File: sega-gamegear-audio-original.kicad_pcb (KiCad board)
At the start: 2 copper layers, 57 x 31 mm, 22 parts, among them CN1 292161-6, CN2 CONN 2P, IC1 TDA2822D, J1 CONN MINI JACK

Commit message: update production files
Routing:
- net Net-(IC1-+I1): track 82.3 -> 81.7 mm
- net Net-(IC1-+I2): track 85.7 -> 85.2 mm
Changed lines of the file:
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@@
     (property "Sheetfile" "sega-gamegear-audio-original.kicad_sch")
     (property "Sheetname" "")
-    (attr through_hole exclude_from_pos_files)
+    (attr through_hole)
     (fp_text reference "CN1" (at -14 0.1) (layer "F.SilkS")
         (effects (font (size 1 1) (thickness 0.2) bold))
@@
     (property "Sheetfile" "sega-gamegear-audio-original.kicad_sch")
     (property "Sheetname" "")
-    (attr through_hole exclude_from_pos_files)
+    (attr through_hole)
     (fp_text reference "CN2" (at 0.9 2.9) (layer "F.SilkS")
         (effects (font (size 1 1) (thickness 0.2) bold))
@@
   (segment (start 70.264471 123.184471) (end 70.28 123.2) (width 0.25) (layer "F.Cu") (net 8))
   (segment (start 70.264471 121.6) (end 70.264471 123.184471) (width 0.57) (layer "F.Cu") (net 8))
-  (segment (start 99.07 118.581056) (end 99.069999 128.600945) (width 0.57) (layer "F.Cu") (net 9))
+  (segment (start 95.788944 115.3) (end 99.07 118.581056) (width 0.57) (layer "F.Cu") (net 9))
   (segment (start 86.50755 113.5695) (end 86.50755 114.70755) (width 0.57) (layer "F.Cu") (net 9))
   (segment (start 70.051056 127.44) (end 66.96211 127.439998) (width 0.57) (layer "F.Cu") (net 9))
+  (segment (start 58.622112 119.1) (end 51.1 119.1) (width 0.57) (layer "F.Cu") (net 9))
+  (segment (start 86.50755 114.70755) (end 87.1 115.3) (width 0.57) (layer "F.Cu") (net 9))
+  (segment (start 99.069999 127.618945) (end 96.848946 129.839998) (width 0.57) (layer "F.Cu") (net 9))
+  (segment (start 66.96211 127.439998) (end 58.622112 119.1) (width 0.57) (layer "F.Cu") (net 9))
+  (segment (start 99.07 118.581056) (end 99.069999 127.618945) (width 0.57) (layer "F.Cu") (net 9))
+  (segment (start 96.848946 129.839998) (end 72.451054 129.839998) (width 0.57) (layer "F.Cu") (net 9))
   (segment (start 72.451054 129.839998) (end 70.051056 127.44) (width 0.57) (layer "F.Cu") (net 9))
-  (segment (start 97.830946 129.839998) (end 72.451054 129.839998) (width 0.57) (layer "F.Cu") (net 9))
-  (segment (start 95.788944 115.3) (end 99.07 118.581056) (width 0.57) (layer "F.Cu") (net 9))
+  (segment (start 49 117) (end 49 112.5) (width 0.57) (layer "F.Cu") (net 9))
   (segment (start 87.1 115.3) (end 95.788944 115.3) (width 0.57) (layer "F.Cu") (net 9))
-  (segment (start 58.622112 119.1) (end 51.1 119.1) (width 0.57) (layer "F.Cu") (net 9))
-  (segment (start 49 117) (end 49 112.5) (width 0.57) (layer "F.Cu") (net 9))
-  (segment (start 86.50755 114.70755) (end 87.1 115.3) (width 0.57) (layer "F.Cu") (net 9))
-  (segment (start 66.96211 127.439998) (end 58.622112 119.1) (width 0.57) (layer "F.Cu") (net 9))
   (segment (start 51.1 119.1) (end 49 117) (width 0.57) (layer "F.Cu") (net 9))
-  (segment (start 99.069999 128.600945) (end 97.830946 129.839998) (width 0.57) (layer "F.Cu") (net 9))
-  (segment (start 98.3 118.9) (end 98.3 128.282) (width 0.57) (layer "F.Cu") (net 10))
-  (segment (start 58.911056 118.3) (end 52.4 118.3) (width 0.57) (layer "F.Cu") (net 10))
-  (segment (start 86.781055 116.069999) (end 95.47 116.07) (width 0.57) (layer "F.Cu") (net 10))
+  (segment (start 98.3 118.9) (end 98.3 127.3) (width 0.57) (layer "F.Cu") (net 10))
   (segment (start 85.24755 114.536494) (end 86.781055 116.069999) (width 0.57) (layer "F.Cu") (net 10))
+  (segment (start 96.530001 129.069999) (end 72.769999 129.069999) (width 0.57) (layer "F.Cu") (net 10))
   (segment (start 70.37 126.67) (end 67.281055 126.669999) (width 0.57) (layer "F.Cu") (net 10))
   (segment (start 85.24755 113.5695) (end 85.24755 114.536494) (width 0.57) (layer "F.Cu") (net 10))
   (segment (start 52.4 118.3) (end 51 116.9) (width 0.57) (layer "F.Cu") (net 10))
-  (segment (start 72.769999 129.069999) (end 70.37 126.67) (width 0.57) (layer "F.Cu") (net 10))
-  (segment (start 98.3 128.282) (end 97.512001 129.069999) (width 0.57) (layer "F.Cu") (net 10))
   (segment (start 67.281055 126.669999) (end 58.911056 118.3) (width 0.57) (layer "F.Cu") (net 10))
   (segment (start 95.47 116.07) (end 98.3 118.9) (width 0.57) (layer "F.Cu") (net 10))
   (segment (start 51 116.9) (end 51 112.5) (width 0.57) (layer "F.Cu") (net 10))
-  (segment (start 97.512001 129.069999) (end 72.769999 129.069999) (width 0.57) (layer "F.Cu") (net 10))
+  (segment (start 58.911056 118.3) (end 52.4 118.3) (width 0.57) (layer "F.Cu") (net 10))
+  (segment (start 98.3 127.3) (end 96.530001 129.069999) (width 0.57) (layer "F.Cu") (net 10))
+  (segment (start 86.781055 116.069999) (end 95.47 116.07) (width 0.57) (layer "F.Cu") (net 10))
+  (segment (start 72.769999 129.069999) (end 70.37 126.67) (width 0.57) (layer "F.Cu") (net 10))
   (segment (start 70.28 120) (end 64.966832 120) (width 0.57) (layer "F.Cu") (net 11))
   (segment (start 59.8 114.833168) (end 59.8 107.7) (width 0.57) (layer "F.Cu") (net 11))

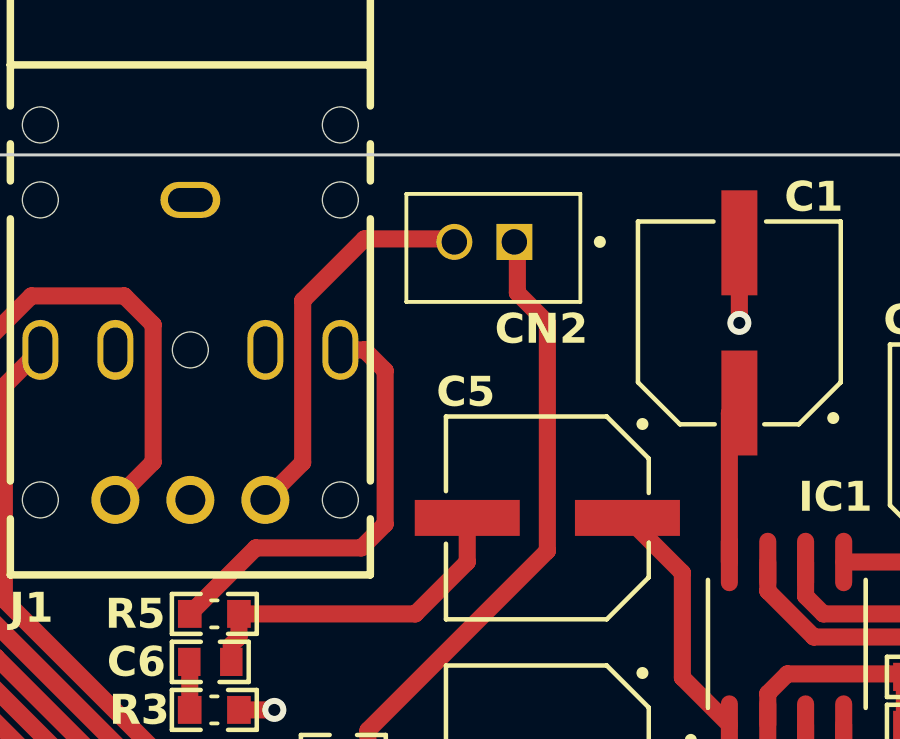
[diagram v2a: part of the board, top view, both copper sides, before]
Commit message: fixes #6
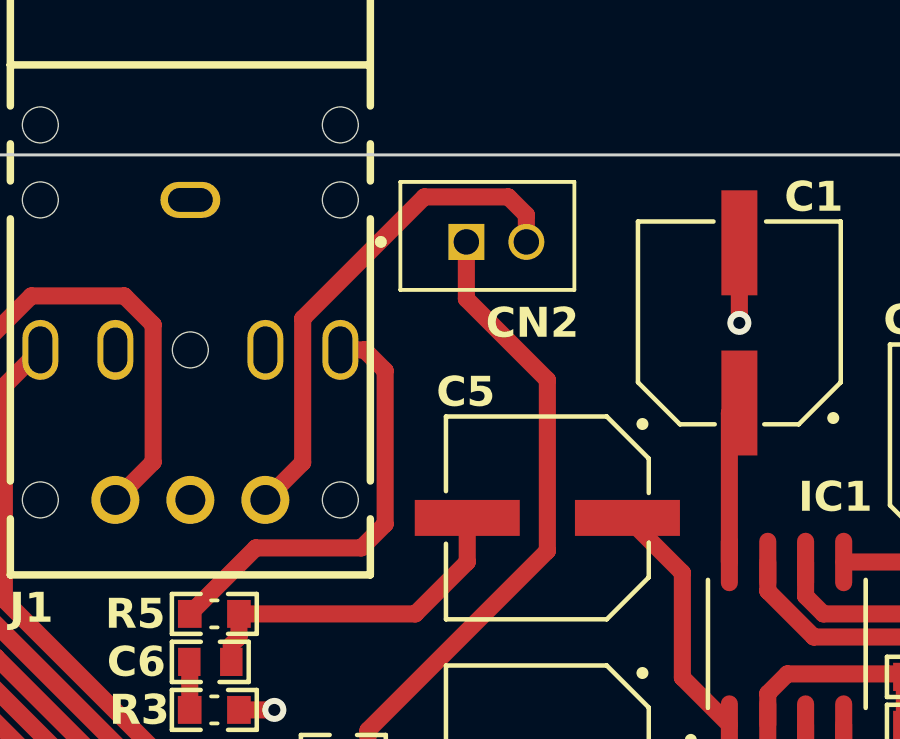
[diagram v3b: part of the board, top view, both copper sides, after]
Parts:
- moved CN2 1.60 mm to (75.2, 102.9), turned to 180 degrees
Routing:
- net Net-(CN2-SP-): track 13.2 -> 16.8 mm
- net Net-(CN2-SP+): track 25.7 -> 26.3 mm
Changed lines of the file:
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@@
     (at 55 115.4 90)
     (property "LCSC Part" "C705785")
-    (property "Manufacturer_Part_Number" "RT0603BRD07100RL")
+    (property "Manufacturer_Part_Number" "RT0603BRD0756KL")
     (property "Sheetfile" "sega-gamegear-audio-original.kicad_sch")
     (property "Sheetname" "")
@@
     (at 92.7 109.7 90)
     (property "Height" "7.8")
-    (property "LCSC Part" "C494824")
+    (property "LCSC Part" "C178540")
     (property "Manufacturer_Name" "Panasonic")
-    (property "Manufacturer_Part_Number" "EEEFN1E101UP")
+    (property "Manufacturer_Part_Number" "EEEFK1E101SP")
     (property "Sheetfile" "sega-gamegear-audio-original.kicad_sch")
     (property "Sheetname" "")
@@
     (property "Sheetfile" "sega-gamegear-audio-original.kicad_sch")
     (property "Sheetname" "")
-    (attr through_hole exclude_from_pos_files exclude_from_bom)
+    (attr through_hole exclude_from_pos_files)
     (fp_text reference "J1" (at 8.6 5.3) (layer "F.SilkS")
         (effects (font (size 1 1) (thickness 0.2) bold))
@@
     (at 84.3 105.6 90)
     (property "Height" "7.8")
-    (property "LCSC Part" "C494824")
+    (property "LCSC Part" "C178540")
     (property "Manufacturer_Name" "Panasonic")
-    (property "Manufacturer_Part_Number" "EEEFN1E101UP")
+    (property "Manufacturer_Part_Number" "EEEFK1E101SP")
     (property "Sheetfile" "sega-gamegear-audio-original.kicad_sch")
     (property "Sheetname" "")
@@
     (property "ki_description" "Panasonic EVUTV2B19A14")
     (property "ki_keywords" "resistor variable")
-    (attr smd exclude_from_pos_files exclude_from_bom)
+    (attr smd exclude_from_pos_files)
     (fp_text reference "VR1" (at -3.4 12 unlocked) (layer "F.SilkS")
         (effects (font (size 1 1) (thickness 0.2) bold))
@@
     (at 66.799664 118.5 180)
     (property "LCSC Part" "C861448")
-    (property "Manufacturer_Part_Number" "RT0603BRD07100RL")
+    (property "Manufacturer_Part_Number" "RT0603BRD074R7L")
     (property "Sheetfile" "sega-gamegear-audio-original.kicad_sch")
     (property "Sheetname" "")
@@
     (at 53 115.4 90)
     (property "LCSC Part" "C705785")
-    (property "Manufacturer_Part_Number" "RT0603BRD07100RL")
+    (property "Manufacturer_Part_Number" "RT0603BRD0756KL")
     (property "Sheetfile" "sega-gamegear-audio-original.kicad_sch")
     (property "Sheetname" "")
@@
     (at 71.1 123.2 180)
     (property "LCSC Part" "C861448")
-    (property "Manufacturer_Part_Number" "RT0603BRD07100RL")
+    (property "Manufacturer_Part_Number" "RT0603BRD074R7L")
     (property "Sheetfile" "sega-gamegear-audio-original.kicad_sch")
     (property "Sheetname" "")
@@
     )
   )
-  (footprint "Sega GameGear Audio Board Original:292161-2" locked (layer "F.Cu")
-    (at 76.8 102.9)
+  (footprint "Sega GameGear Audio Board Original:292161-2" (layer "F.Cu")
+    (at 75.2 102.9 180)
     (property "LCSC Part" "C86484")
     (property "Manufacturer_Part_Number" "292161-2")
@@
     (property "Sheetname" "")
     (attr through_hole)
-    (fp_text reference "CN2" (at 0.9 2.9) (layer "F.SilkS")
+    (fp_text reference "CN2" (at -2.2 -2.7) (layer "F.SilkS")
         (effects (font (size 1 1) (thickness 0.2) bold))
     )
@@
     (fp_circle (center 2.85 0) (end 2.95 0)
       (stroke (width 0.2) (type solid)) (fill none) (layer "F.Fab"))
-    (pad "1" thru_hole rect locked (at 0 0) (size 1.2 1.2) (drill 0.85) (layers "*.Cu" "*.Mask")
+    (pad "1" thru_hole rect (at 0 0 180) (size 1.2 1.2) (drill 0.85) (layers "*.Cu" "*.Mask")
       (net 18 "Net-(CN2-SP+)") (pinfunction "SP+") (pintype "passive") (solder_mask_margin 0.102))
-    (pad "2" thru_hole circle locked (at -2 0) (size 1.2 1.2) (drill 0.85) (layers "*.Cu" "*.Mask")
+    (pad "2" thru_hole circle (at -2 0 180) (size 1.2 1.2) (drill 0.85) (layers "*.Cu" "*.Mask")
       (net 23 "Net-(CN2-SP-)") (pinfunction "SP-") (pintype "passive") (solder_mask_margin 0.102))
     (model "${KIPRJMOD}/libraries/3dmodels/292161-2.stp"
@@
   (segment (start 73 127) (end 74.3 128.3) (width 0.57) (layer "F.Cu") (net 17))
   (segment (start 74.3 128.3) (end 88.312 128.3) (width 0.57) (layer "F.Cu") (net 17))
+  (segment (start 75.2 104.8) (end 75.2 102.9) (width 0.57) (layer "F.Cu") (net 18))
+  (segment (start 77.9 107.5) (end 75.2 104.8) (width 0.57) (layer "F.Cu") (net 18))
   (segment (start 71.92 119.98) (end 71.82 119.88) (width 0.57) (layer "F.Cu") (net 18))
   (segment (start 71.664471 121.6) (end 71.664471 120.935529) (width 0.57) (layer "F.Cu") (net 18))
   (segment (start 71.92 120) (end 71.92 119.18) (width 0.57) (layer "F.Cu") (net 18))
+  (segment (start 77.9 113.2) (end 77.9 107.5) (width 0.57) (layer "F.Cu") (net 18))
   (segment (start 71.92 120.68) (end 71.92 119.98) (width 0.57) (layer "F.Cu") (net 18))
   (segment (start 75.23 120.4) (end 73.3 120.4) (width 0.57) (layer "F.Cu") (net 18))
   (segment (start 71.664471 120.935529) (end 71.92 120.68) (width 0.57) (layer "F.Cu") (net 18))
   (segment (start 75.23 120.6) (end 75.03 120.4) (width 0.57) (layer "F.Cu") (net 18))
-  (segment (start 77.9 105.6) (end 76.9 104.6) (width 0.57) (layer "F.Cu") (net 18))
+  (segment (start 71.92 119.18) (end 77.9 113.2) (width 0.57) (layer "F.Cu") (net 18))
   (segment (start 72.9 120) (end 71.92 120) (width 0.57) (layer "F.Cu") (net 18))
-  (segment (start 71.92 119.18) (end 77.9 113.2) (width 0.57) (layer "F.Cu") (net 18))
   (segment (start 73.3 120.4) (end 72.9 120) (width 0.57) (layer "F.Cu") (net 18))
-  (segment (start 76.9 104.6) (end 76.9 102.8) (width 0.57) (layer "F.Cu") (net 18))
-  (segment (start 77.9 113.2) (end 77.9 105.6) (width 0.57) (layer "F.Cu") (net 18))
   (segment (start 53 116.22) (end 54.28 117.5) (width 0.57) (layer "F.Cu") (net 19))
   (segment (start 59.2 117.5) (end 67.6 125.9) (width 0.57) (layer "F.Cu") (net 19))
@@
   (segment (start 68.237888 124.36) (end 80.36 124.36) (width 0.57) (layer "F.Cu") (net 22))
   (segment (start 64.75894 110.24106) (end 64.75894 105.65894) (width 0.57) (layer "F.Cu") (net 22))
+  (segment (start 73.8 101.4) (end 76.6 101.4) (width 0.57) (layer "F.Cu") (net 23))
   (segment (start 68.5 111.5) (end 69.744757 110.255243) (width 0.57) (layer "F.Cu") (net 23))
-  (segment (start 69.744757 104.855243) (end 71.8 102.8) (width 0.57) (layer "F.Cu") (net 23))
-  (segment (start 69.744757 110.255243) (end 69.744757 104.855243) (width 0.57) (layer "F.Cu") (net 23))
-  (segment (start 71.8 102.8) (end 74.9 102.8) (width 0.57) (layer "F.Cu") (net 23))
+  (segment (start 69.744757 105.455243) (end 73.8 101.4) (width 0.57) (layer "F.Cu") (net 23))
+  (segment (start 69.744757 110.255243) (end 69.744757 105.455243) (width 0.57) (layer "F.Cu") (net 23))
+  (segment (start 76.6 101.4) (end 77.2 102) (width 0.57) (layer "F.Cu") (net 23))
+  (segment (start 77.2 102) (end 77.2 102.9) (width 0.57) (layer "F.Cu") (net 23))
   (zone (net 2) (net_name "GND") (layer "B.Cu") (hatch edge 0.5)
     (connect_pads (clearance 0.5))
